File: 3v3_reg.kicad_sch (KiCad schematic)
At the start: 13 parts, among them U1 BD9G341AEFJ

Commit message: Changed 5V regulator and 12V regulator to the SiC461. Both support 10A and 5V and 12V respectively
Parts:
- renumbered D1 to D5, R6 to R10, R1 to R5, R2 to R6, R3 to R7, R4 to R8, R5 to R9
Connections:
- net Vin renamed V_IN
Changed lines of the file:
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@@
     (effects (font (size 1.27 1.27)) (justify right))
   )
-  (hierarchical_label "Vin" (shape input) (at 88.9 90.17 180) (fields_autoplaced)
+  (hierarchical_label "V_IN" (shape input) (at 88.9 90.17 180) (fields_autoplaced)
     (effects (font (size 1.27 1.27)) (justify right))
   )
@@
         )
         (path "/530b9f5d-4c5f-47a4-a889-3cce870d311f/eea42af5-9968-489d-9acf-9145a737deb9"
-          (reference "C31") (unit 1)
+          (reference "C47") (unit 1)
         )
       )
@@
         )
         (path "/530b9f5d-4c5f-47a4-a889-3cce870d311f/eea42af5-9968-489d-9acf-9145a737deb9"
-          (reference "C30") (unit 1)
+          (reference "C46") (unit 1)
         )
       )
@@
   (symbol (lib_id "Device:R_US") (at 106.68 102.87 0) (unit 1)
     (in_bom yes) (on_board yes) (dnp no) (fields_autoplaced)
-    (property "Reference" "R2" (at 109.22 102.235 0)
+    (property "Reference" "R6" (at 109.22 102.235 0)
       (effects (font (size 1.27 1.27)) (justify left))
     )
@@
       (project "crush-power-board"
         (path "/530b9f5d-4c5f-47a4-a889-3cce870d311f/5ebfd0d2-e05a-44c8-bc6b-7dbf219b0053"
-          (reference "R2") (unit 1)
-        )
-        (path "/530b9f5d-4c5f-47a4-a889-3cce870d311f/eea42af5-9968-489d-9acf-9145a737deb9"
-          (reference "R20") (unit 1)
+          (reference "R6") (unit 1)
+        )
+        (path "/530b9f5d-4c5f-47a4-a889-3cce870d311f/eea42af5-9968-489d-9acf-9145a737deb9"
+          (reference "R34") (unit 1)
         )
       )
@@
         )
         (path "/530b9f5d-4c5f-47a4-a889-3cce870d311f/eea42af5-9968-489d-9acf-9145a737deb9"
-          (reference "C32") (unit 1)
+          (reference "C48") (unit 1)
         )
       )
@@
         )
         (path "/530b9f5d-4c5f-47a4-a889-3cce870d311f/eea42af5-9968-489d-9acf-9145a737deb9"
-          (reference "C29") (unit 1)
+          (reference "C45") (unit 1)
         )
       )
@@
   (symbol (lib_id "Device:D_Schottky") (at 147.32 92.71 270) (unit 1)
     (in_bom yes) (on_board yes) (dnp no) (fields_autoplaced)
-    (property "Reference" "D1" (at 149.86 91.7575 90)
+    (property "Reference" "D5" (at 149.86 91.7575 90)
       (effects (font (size 1.27 1.27)) (justify left))
     )
@@
       (project "crush-power-board"
         (path "/530b9f5d-4c5f-47a4-a889-3cce870d311f/5ebfd0d2-e05a-44c8-bc6b-7dbf219b0053"
-          (reference "D1") (unit 1)
-        )
-        (path "/530b9f5d-4c5f-47a4-a889-3cce870d311f/eea42af5-9968-489d-9acf-9145a737deb9"
-          (reference "D2") (unit 1)
+          (reference "D5") (unit 1)
+        )
+        (path "/530b9f5d-4c5f-47a4-a889-3cce870d311f/eea42af5-9968-489d-9acf-9145a737deb9"
+          (reference "D6") (unit 1)
         )
       )
@@
   (symbol (lib_id "Device:R_US") (at 130.81 123.19 0) (unit 1)
     (in_bom yes) (on_board yes) (dnp no) (fields_autoplaced)
-    (property "Reference" "R3" (at 133.35 122.555 0)
+    (property "Reference" "R7" (at 133.35 122.555 0)
       (effects (font (size 1.27 1.27)) (justify left))
     )
@@
       (project "crush-power-board"
         (path "/530b9f5d-4c5f-47a4-a889-3cce870d311f/5ebfd0d2-e05a-44c8-bc6b-7dbf219b0053"
-          (reference "R3") (unit 1)
-        )
-        (path "/530b9f5d-4c5f-47a4-a889-3cce870d311f/eea42af5-9968-489d-9acf-9145a737deb9"
-          (reference "R21") (unit 1)
+          (reference "R7") (unit 1)
+        )
+        (path "/530b9f5d-4c5f-47a4-a889-3cce870d311f/eea42af5-9968-489d-9acf-9145a737deb9"
+          (reference "R35") (unit 1)
         )
       )
@@
   (symbol (lib_id "Device:R_US") (at 180.34 95.25 0) (unit 1)
     (in_bom yes) (on_board yes) (dnp no) (fields_autoplaced)
-    (property "Reference" "R5" (at 182.88 94.615 0)
+    (property "Reference" "R9" (at 182.88 94.615 0)
       (effects (font (size 1.27 1.27)) (justify left))
     )
@@
       (project "crush-power-board"
         (path "/530b9f5d-4c5f-47a4-a889-3cce870d311f/5ebfd0d2-e05a-44c8-bc6b-7dbf219b0053"
-          (reference "R5") (unit 1)
-        )
-        (path "/530b9f5d-4c5f-47a4-a889-3cce870d311f/eea42af5-9968-489d-9acf-9145a737deb9"
-          (reference "R23") (unit 1)
+          (reference "R9") (unit 1)
+        )
+        (path "/530b9f5d-4c5f-47a4-a889-3cce870d311f/eea42af5-9968-489d-9acf-9145a737deb9"
+          (reference "R37") (unit 1)
         )
       )
@@
   (symbol (lib_id "Device:R_US") (at 106.68 93.98 0) (unit 1)
     (in_bom yes) (on_board yes) (dnp no) (fields_autoplaced)
-    (property "Reference" "R1" (at 109.22 93.345 0)
+    (property "Reference" "R5" (at 109.22 93.345 0)
       (effects (font (size 1.27 1.27)) (justify left))
     )
@@
       (project "crush-power-board"
         (path "/530b9f5d-4c5f-47a4-a889-3cce870d311f/5ebfd0d2-e05a-44c8-bc6b-7dbf219b0053"
-          (reference "R1") (unit 1)
-        )
-        (path "/530b9f5d-4c5f-47a4-a889-3cce870d311f/eea42af5-9968-489d-9acf-9145a737deb9"
-          (reference "R19") (unit 1)
+          (reference "R5") (unit 1)
+        )
+        (path "/530b9f5d-4c5f-47a4-a889-3cce870d311f/eea42af5-9968-489d-9acf-9145a737deb9"
+          (reference "R33") (unit 1)
         )
       )
@@
   (symbol (lib_id "Device:R_US") (at 149.86 121.92 0) (unit 1)
     (in_bom yes) (on_board yes) (dnp no) (fields_autoplaced)
-    (property "Reference" "R4" (at 152.4 121.285 0)
+    (property "Reference" "R8" (at 152.4 121.285 0)
       (effects (font (size 1.27 1.27)) (justify left))
     )
@@
       (project "crush-power-board"
         (path "/530b9f5d-4c5f-47a4-a889-3cce870d311f/5ebfd0d2-e05a-44c8-bc6b-7dbf219b0053"
-          (reference "R4") (unit 1)
-        )
-        (path "/530b9f5d-4c5f-47a4-a889-3cce870d311f/eea42af5-9968-489d-9acf-9145a737deb9"
-          (reference "R22") (unit 1)
+          (reference "R8") (unit 1)
+        )
+        (path "/530b9f5d-4c5f-47a4-a889-3cce870d311f/eea42af5-9968-489d-9acf-9145a737deb9"
+          (reference "R36") (unit 1)
         )
       )
@@
   (symbol (lib_id "Device:R_US") (at 180.34 105.41 0) (unit 1)
     (in_bom yes) (on_board yes) (dnp no) (fields_autoplaced)
-    (property "Reference" "R6" (at 182.88 104.775 0)
+    (property "Reference" "R10" (at 182.88 104.775 0)
       (effects (font (size 1.27 1.27)) (justify left))
     )
@@
       (project "crush-power-board"
         (path "/530b9f5d-4c5f-47a4-a889-3cce870d311f/5ebfd0d2-e05a-44c8-bc6b-7dbf219b0053"
-          (reference "R6") (unit 1)
-        )
-        (path "/530b9f5d-4c5f-47a4-a889-3cce870d311f/eea42af5-9968-489d-9acf-9145a737deb9"
-          (reference "R24") (unit 1)
-        )
-      )
+          (reference "R10") (unit 1)
+        )
+        (path "/530b9f5d-4c5f-47a4-a889-3cce870d311f/eea42af5-9968-489d-9acf-9145a737deb9"
+          (reference "R38") (unit 1)
+        )
+      )

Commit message: Changed schottky diode for 3.3V regulator
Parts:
- D5: value RB095BGE-90TL -> SS36-E3/57T; footprint crush-power-footprints:DIO_RR601BM4_ROM-L -> crush-power-footprints:DIODE_DO214AB
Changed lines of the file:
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@@
       (effects (font (size 1.27 1.27)) (justify left))
     )
-    (property "Value" "RB095BGE-90TL" (at 149.86 94.2975 90)
+    (property "Value" "SS36-E3/57T" (at 149.86 94.2975 90)
       (effects (font (size 1.27 1.27)) (justify left))
     )
-    (property "Footprint" "crush-power-footprints:DIO_RR601BM4_ROM-L" (at 147.32 92.71 0)
+    (property "Footprint" "crush-power-footprints:DIODE_DO214AB" (at 147.32 92.71 0)
       (effects (font (size 1.27 1.27)) hide)
     )

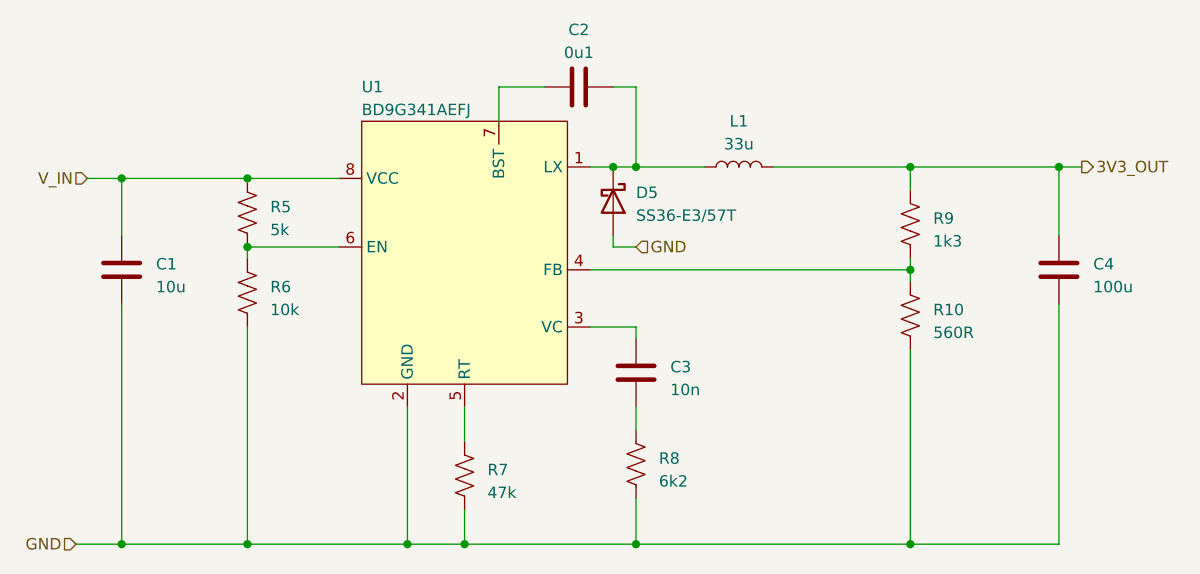
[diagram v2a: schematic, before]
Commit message: drc fixes and update schematic to reflect correct ic footprints
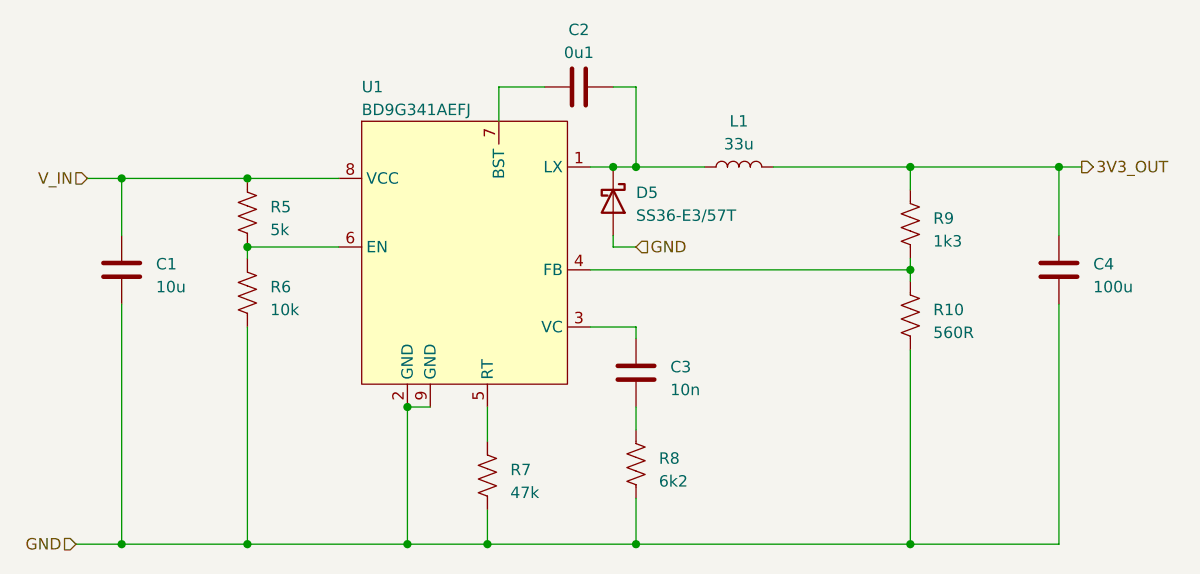
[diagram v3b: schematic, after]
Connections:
- net GND: now also U1.9 (GND)
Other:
- moved on the sheet: R7
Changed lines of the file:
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@@
   (junction (at 149.86 88.9) (diameter 0) (color 0 0 0 0)
   )
+  (junction (at 133.35 130.81) (diameter 0) (color 0 0 0 0)
+  )
   (junction (at 92.71 90.17) (diameter 0) (color 0 0 0 0)
   )
+  (junction (at 124.46 115.57) (diameter 0) (color 0 0 0 0)
+  )
   (junction (at 180.34 130.81) (diameter 0) (color 0 0 0 0)
   )
@@
   (junction (at 180.34 100.33) (diameter 0) (color 0 0 0 0)
   )
-  (junction (at 130.81 130.81) (diameter 0) (color 0 0 0 0)
-  )
   (junction (at 106.68 90.17) (diameter 0) (color 0 0 0 0)
   )
@@
     (stroke (width 0) (type default))
   )
-  (wire (pts (xy 130.81 130.81) (xy 124.46 130.81))
-    (stroke (width 0) (type default))
-  )
   (wire (pts (xy 180.34 88.9) (xy 196.85 88.9))
     (stroke (width 0) (type default))
@@
     (stroke (width 0) (type default))
   )
+  (wire (pts (xy 124.46 115.57) (xy 127 115.57))
+    (stroke (width 0) (type default))
+  )
   (wire (pts (xy 147.32 88.9) (xy 149.86 88.9))
     (stroke (width 0) (type default))
@@
     (stroke (width 0) (type default))
   )
-  (wire (pts (xy 130.81 130.81) (xy 149.86 130.81))
+  (wire (pts (xy 124.46 130.81) (xy 133.35 130.81))
     (stroke (width 0) (type default))
   )
@@
     (stroke (width 0) (type default))
   )
-  (wire (pts (xy 130.81 115.57) (xy 130.81 119.38))
+  (wire (pts (xy 133.35 115.57) (xy 133.35 119.38))
     (stroke (width 0) (type default))
   )
@@
     (stroke (width 0) (type default))
   )
+  (wire (pts (xy 133.35 130.81) (xy 149.86 130.81))
+    (stroke (width 0) (type default))
+  )
   (wire (pts (xy 144.78 100.33) (xy 180.34 100.33))
     (stroke (width 0) (type default))
@@
     (stroke (width 0) (type default))
   )
-  (wire (pts (xy 130.81 127) (xy 130.81 130.81))
+  (wire (pts (xy 133.35 127) (xy 133.35 130.81))
     (stroke (width 0) (type default))
   )
@@
     )
   )
-  (symbol (lib_id "Device:R_US") (at 130.81 123.19 0) (unit 1)
-    (in_bom yes) (on_board yes) (dnp no) (fields_autoplaced)
-    (property "Reference" "R7" (at 133.35 122.555 0)
-      (effects (font (size 1.27 1.27)) (justify left))
-    )
-    (property "Value" "47k" (at 133.35 125.095 0)
-      (effects (font (size 1.27 1.27)) (justify left))
-    )
-    (property "Footprint" "Resistor_SMD:R_0603_1608Metric" (at 131.826 123.444 90)
-      (effects (font (size 1.27 1.27)) hide)
-    )
-    (property "Datasheet" "~" (at 130.81 123.19 0)
+  (symbol (lib_id "Device:R_US") (at 133.35 123.19 0) (unit 1)
+    (in_bom yes) (on_board yes) (dnp no) (fields_autoplaced)
+    (property "Reference" "R7" (at 135.89 122.555 0)
+      (effects (font (size 1.27 1.27)) (justify left))
+    )
+    (property "Value" "47k" (at 135.89 125.095 0)
+      (effects (font (size 1.27 1.27)) (justify left))
+    )
+    (property "Footprint" "Resistor_SMD:R_0603_1608Metric" (at 134.366 123.444 90)
+      (effects (font (size 1.27 1.27)) hide)
+    )
+    (property "Datasheet" "~" (at 133.35 123.19 0)
       (effects (font (size 1.27 1.27)) hide)
     )
@@
     (pin "7")
     (pin "8")
-    (instances
-      (project "crush-power-board"
+    (pin "9")
+    (instances
+      (project "crush-power-board"

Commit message: fix footprint on 3v3 output capacitors
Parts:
- C4: footprint Capacitor_SMD:C_0603_1608Metric -> Capacitor_SMD:C_1206_3216Metric
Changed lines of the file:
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@@
       (effects (font (size 1.27 1.27)) (justify left))
     )
-    (property "Footprint" "Capacitor_SMD:C_0603_1608Metric" (at 197.8152 104.14 0)
+    (property "Footprint" "Capacitor_SMD:C_1206_3216Metric" (at 197.8152 104.14 0)
       (effects (font (size 1.27 1.27)) hide)
     )
